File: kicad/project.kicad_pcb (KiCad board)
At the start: 2 copper layers, 77.2 x 94.1 mm, 20 parts, among them J1 Conn_01x01_Socket, J2 Conn_01x02_Socket, U1 NE555P, U2 4017

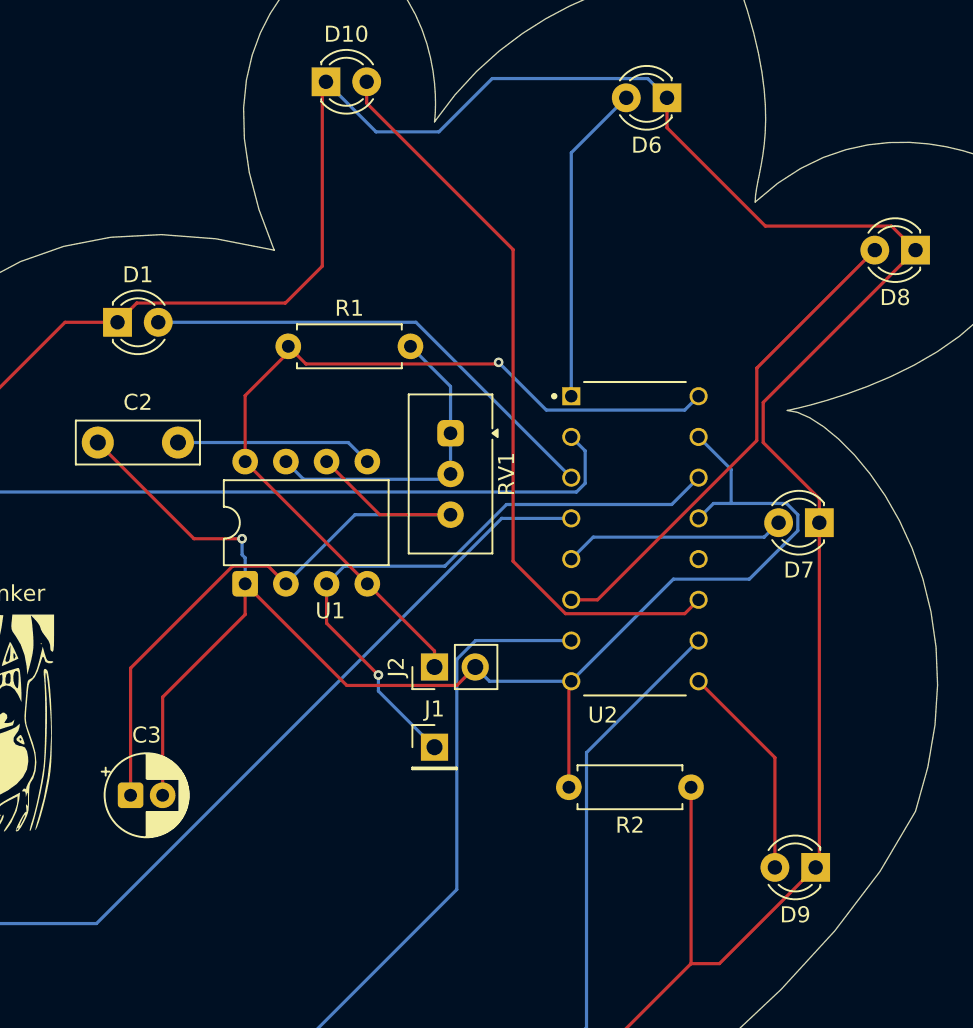
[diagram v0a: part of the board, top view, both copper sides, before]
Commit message: fix: correctly ordered lights
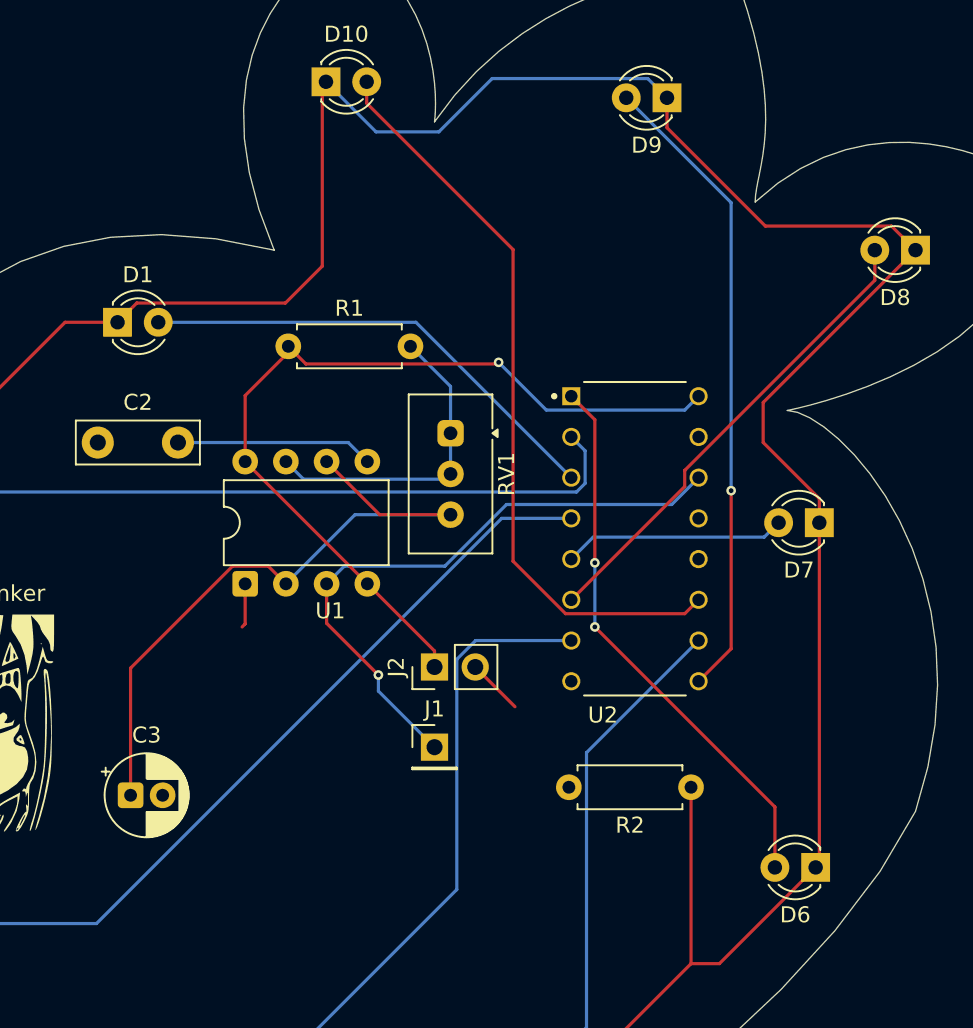
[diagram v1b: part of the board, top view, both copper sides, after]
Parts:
- moved D6 48.9 mm to (181.8, 100.5)
- moved D9 48.9 mm to (172.5, 52.5)
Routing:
- net CTGND: track 91.1 -> 6.28 mm, vias 1 -> 0
- net Net-(D9-A): track 13.6 -> 39.9 mm, vias 0 -> 1
- net Net-(D6-A): track 20.0 -> 34.7 mm, vias 0 -> 2
- net Net-(D8-A): track 30.6 -> 29.7 mm
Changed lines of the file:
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@@
 	(footprint "LED_THT:LED_D3.0mm"
 		(layer "F.Cu")
-		(at 172.5 52.5 180)
+		(at 181.77 100.5 180)
 		(descr "LED, diameter 3.0mm, 2 pins, generated by kicad-footprint-generator")
 		(tags "LED")
@@
 		)
 		(point
-			(at 171.23 52.5)
+			(at 180.5 100.5)
 			(size 2)
 			(layer "F.Fab")
@@
 			(pintype "input")
 			(solder_mask_margin 0.102)
+			(thermal_bridge_angle 0)
 		)
 		(pad "14" thru_hole circle
@@
 	(footprint "LED_THT:LED_D3.0mm"
 		(layer "F.Cu")
-		(at 181.77 100.5 180)
+		(at 172.5 52.5 180)
 		(descr "LED, diameter 3.0mm, 2 pins, generated by kicad-footprint-generator")
 		(tags "LED")
@@
 		)
 		(point
-			(at 180.5 100.5)
+			(at 171.23 52.5)
 			(size 2)
 			(layer "F.Fab")
@@
 	)
 	(segment
-		(start 137 74)
-		(end 143 80)
+		(start 146.19 85.31)
+		(end 146 85.5)
 		(width 0.2)
 		(layer "F.Cu")
@@
 	)
 	(segment
-		(start 166.38 89.04)
-		(end 166.53 88.89)
+		(start 146.19 82.81)
+		(end 146.19 85.31)
 		(width 0.2)
 		(layer "F.Cu")
@@
 	)
 	(segment
-		(start 143 80)
-		(end 146 80)
-		(width 0.2)
-		(layer "F.Cu")
-		(net "CTGND")
-	)
-	(segment
-		(start 152.53 89.15)
-		(end 146.19 82.81)
-		(width 0.2)
-		(layer "F.Cu")
-		(net "CTGND")
-	)
-	(segment
-		(start 166.38 95.5)
-		(end 166.38 89.04)
-		(width 0.2)
-		(layer "F.Cu")
-		(net "CTGND")
-	)
-	(segment
-		(start 146.19 84.73)
-		(end 146.19 82.81)
-		(width 0.2)
-		(layer "F.Cu")
-		(net "CTGND")
-	)
-	(segment
-		(start 141.044888 89.875112)
-		(end 146.19 84.73)
-		(width 0.2)
-		(layer "F.Cu")
-		(net "CTGND")
-	)
-	(segment
-		(start 141.044888 96)
-		(end 141.044888 89.875112)
-		(width 0.2)
-		(layer "F.Cu")
-		(net "CTGND")
-	)
-	(segment
 		(start 160.54 88)
-		(end 159.39 89.15)
-		(width 0.2)
-		(layer "F.Cu")
-		(net "CTGND")
-	)
-	(segment
-		(start 159.39 89.15)
-		(end 152.53 89.15)
-		(width 0.2)
-		(layer "F.Cu")
-		(net "CTGND")
-	)
-	(via
-		(at 146 80)
-		(size 0.6)
-		(drill 0.3)
-		(layers "F.Cu" "B.Cu")
-		(net "CTGND")
-	)
-	(segment
-		(start 180.66 78.502943)
-		(end 179.957057 77.8)
-		(width 0.2)
-		(layer "B.Cu")
-		(net "CTGND")
-	)
-	(segment
-		(start 179.957057 77.8)
-		(end 176.5 77.8)
-		(width 0.2)
-		(layer "B.Cu")
-		(net "CTGND")
-	)
-	(segment
-		(start 177.637057 82.52)
-		(end 180.66 79.497057)
-		(width 0.2)
-		(layer "B.Cu")
-		(net "CTGND")
-	)
-	(segment
-		(start 166.53 88.89)
-		(end 172.9 82.52)
-		(width 0.2)
-		(layer "B.Cu")
-		(net "CTGND")
-	)
-	(segment
-		(start 176.5 77.8)
-		(end 175.4 77.8)
-		(width 0.2)
-		(layer "B.Cu")
-		(net "CTGND")
-	)
-	(segment
-		(start 160.54 88)
-		(end 161.43 88.89)
-		(width 0.2)
-		(layer "B.Cu")
-		(net "CTGND")
-	)
-	(segment
-		(start 146 80)
-		(end 146 81)
-		(width 0.2)
-		(layer "B.Cu")
-		(net "CTGND")
-	)
-	(segment
-		(start 172.9 82.52)
-		(end 177.637057 82.52)
-		(width 0.2)
-		(layer "B.Cu")
-		(net "CTGND")
-	)
-	(segment
-		(start 174.47 73.65)
-		(end 176.5 75.68)
-		(width 0.2)
-		(layer "B.Cu")
-		(net "CTGND")
-	)
-	(segment
-		(start 180.66 79.497057)
-		(end 180.66 78.502943)
-		(width 0.2)
-		(layer "B.Cu")
-		(net "CTGND")
-	)
-	(segment
-		(start 176.5 75.68)
-		(end 176.5 77.8)
-		(width 0.2)
-		(layer "B.Cu")
-		(net "CTGND")
-	)
-	(segment
-		(start 146.19 81.19)
-		(end 146.19 82.81)
-		(width 0.2)
-		(layer "B.Cu")
-		(net "CTGND")
-	)
-	(segment
-		(start 161.43 88.89)
-		(end 166.53 88.89)
-		(width 0.2)
-		(layer "B.Cu")
-		(net "CTGND")
-	)
-	(segment
-		(start 146 81)
-		(end 146.19 81.19)
-		(width 0.2)
-		(layer "B.Cu")
-		(net "CTGND")
-	)
-	(segment
-		(start 175.4 77.8)
-		(end 174.47 78.73)
-		(width 0.2)
-		(layer "B.Cu")
+		(end 163.02 90.48)
+		(width 0.2)
+		(layer "F.Cu")
 		(net "CTGND")
 	)
@@
 	)
 	(segment
-		(start 178.1 69.36)
-		(end 178.1 73.876705)
+		(start 166.53 83.81)
+		(end 166.538529 83.81)
 		(width 0.2)
 		(layer "F.Cu")
@@
 	)
 	(segment
-		(start 168.166705 83.81)
-		(end 166.53 83.81)
+		(start 173.605 75.738295)
+		(end 185.46 63.883295)
 		(width 0.2)
 		(layer "F.Cu")
@@
 	)
 	(segment
-		(start 178.1 73.876705)
-		(end 168.166705 83.81)
+		(start 185.46 63.883295)
+		(end 185.46 62)
 		(width 0.2)
 		(layer "F.Cu")
@@
 	)
 	(segment
-		(start 185.46 62)
-		(end 178.1 69.36)
+		(start 173.605 76.743529)
+		(end 173.605 75.738295)
 		(width 0.2)
 		(layer "F.Cu")
@@
 	)
 	(segment
-		(start 169.96 52.5)
-		(end 166.53 55.93)
-		(width 0.2)
-		(layer "B.Cu")
+		(start 166.538529 83.81)
+		(end 173.605 76.743529)
+		(width 0.2)
+		(layer "F.Cu")
+		(net "Net-(D8-A)")
+	)
+	(segment
+		(start 168 72.58)
+		(end 166.53 71.11)
+		(width 0.2)
+		(layer "F.Cu")
 		(net "Net-(D6-A)")
 	)
 	(segment
-		(start 166.53 55.93)
-		(end 166.53 71.11)
+		(start 179.23 96.73)
+		(end 168 85.5)
+		(width 0.2)
+		(layer "F.Cu")
+		(net "Net-(D6-A)")
+	)
+	(segment
+		(start 179.23 100.5)
+		(end 179.23 96.73)
+		(width 0.2)
+		(layer "F.Cu")
+		(net "Net-(D6-A)")
+	)
+	(segment
+		(start 168 81.5)
+		(end 168 72.58)
+		(width 0.2)
+		(layer "F.Cu")
+		(net "Net-(D6-A)")
+	)
+	(via
+		(at 168 81.5)
+		(size 0.6)
+		(drill 0.3)
+		(layers "F.Cu" "B.Cu")
+		(net "Net-(D6-A)")
+	)
+	(via
+		(at 168 85.5)
+		(size 0.6)
+		(drill 0.3)
+		(layers "F.Cu" "B.Cu")
+		(net "Net-(D6-A)")
+	)
+	(segment
+		(start 168 85.5)
+		(end 168 81.5)
 		(width 0.2)
 		(layer "B.Cu")
@@
 	)
 	(segment
-		(start 179.23 93.65)
-		(end 174.47 88.89)
+		(start 174.47 88.89)
+		(end 176.5 86.86)
 		(width 0.2)
 		(layer "F.Cu")
@@
 	)
 	(segment
-		(start 179.23 100.5)
-		(end 179.23 93.65)
+		(start 176.5 86.86)
+		(end 176.5 77)
 		(width 0.2)
 		(layer "F.Cu")
 		(net "Net-(D9-A)")
 	)
+	(via
+		(at 176.5 77)
+		(size 0.6)
+		(drill 0.3)
+		(layers "F.Cu" "B.Cu")
+		(net "Net-(D9-A)")
+	)
+	(segment
+		(start 176.5 77)
+		(end 176.5 59.04)
+		(width 0.2)
+		(layer "B.Cu")
+		(net "Net-(D9-A)")
+	)
+	(segment
+		(start 176.5 59.04)
+		(end 169.96 52.5)
+		(width 0.2)
+		(layer "B.Cu")
+		(net "Net-(D9-A)")
+	)
